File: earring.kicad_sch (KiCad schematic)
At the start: 104 parts, among them J2 USB_C_Receptacle_USB2.0, Q1 Q_NMOS_SGD, Q5 light_sensor, U1 Magnetic Switch, U10 USBLC6-2P6, U20 LGS4056H, U3 RP2040, U4 W25Q16JVUXIQ, U43 TPS22913BYZVR, U44 TPS22913BYZVR, U7 LSM6DS3, U8 DS6091AED4, U9 NCP730BMT330TBG, Y1 Crystal_GND24

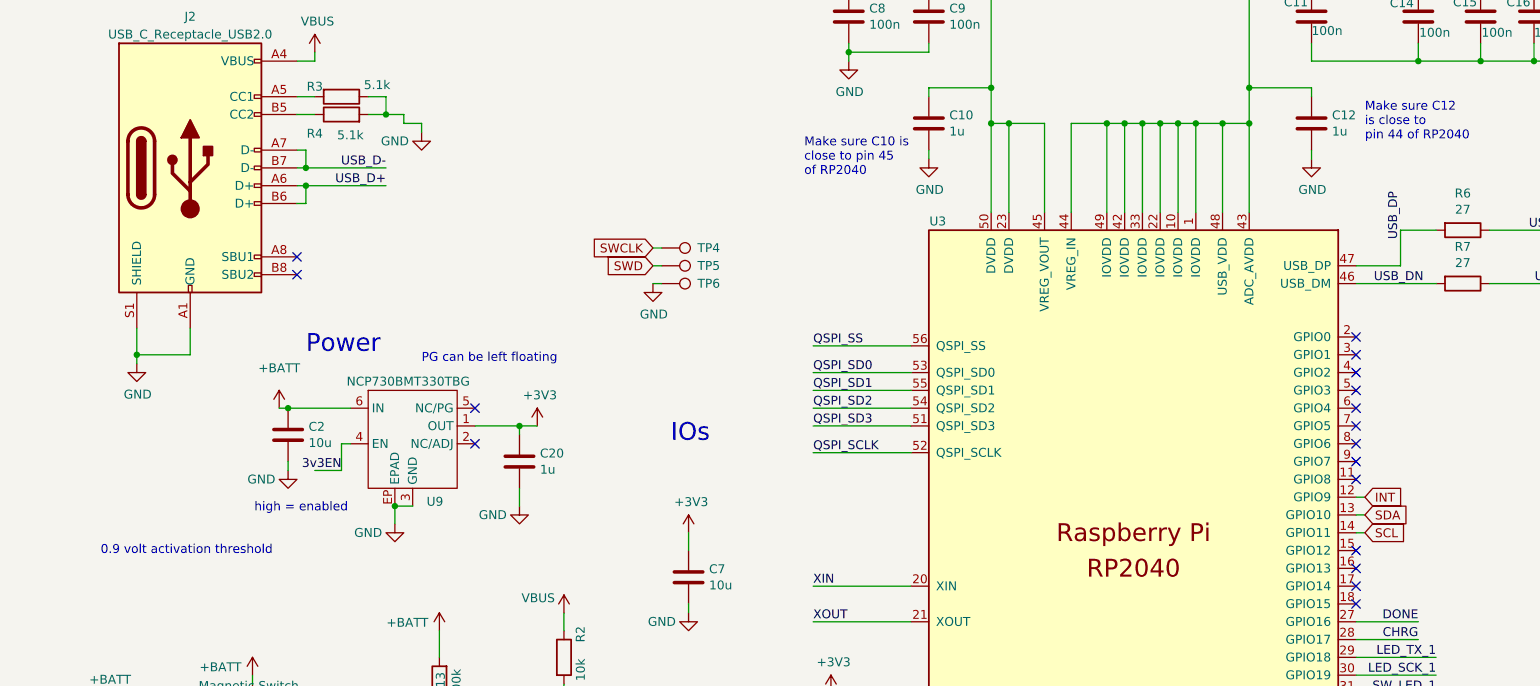
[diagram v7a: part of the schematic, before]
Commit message: updated with better clearance, ordered this rev after canceling the last order
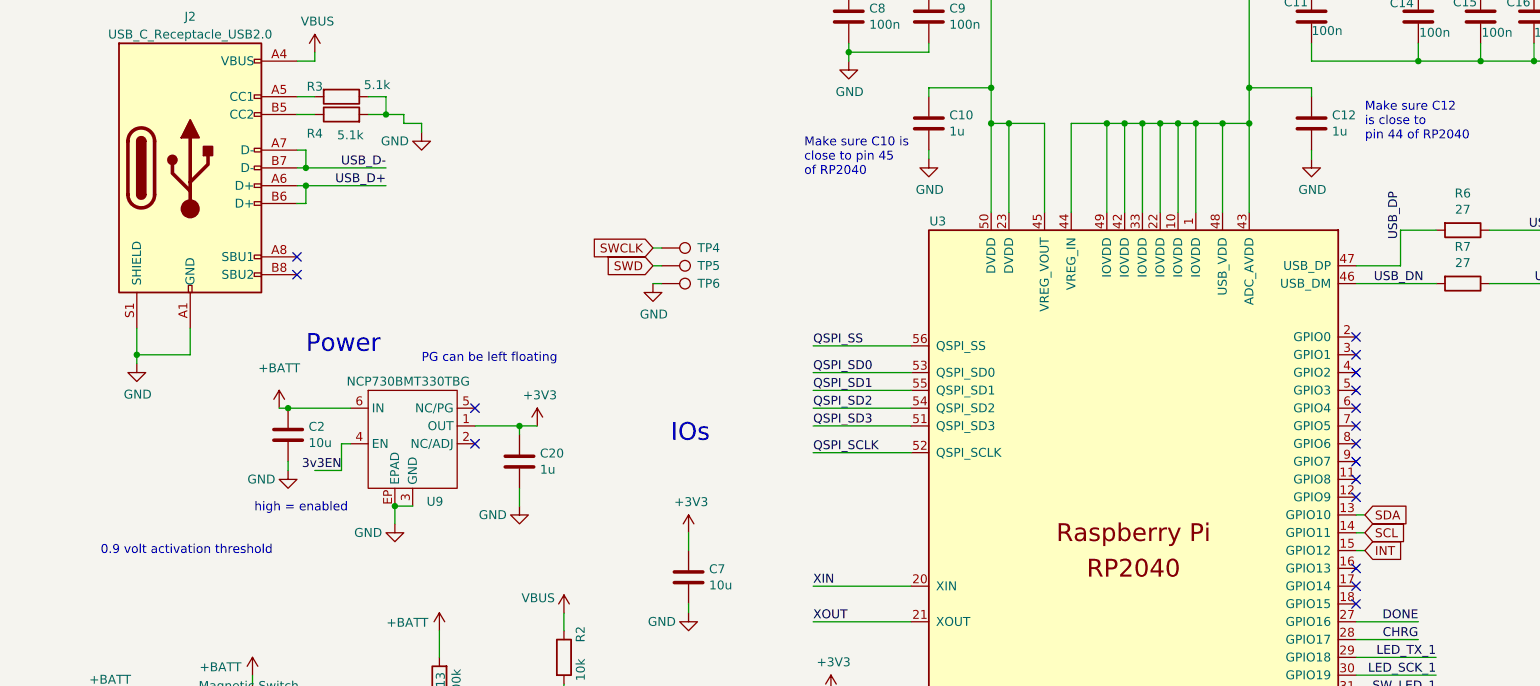
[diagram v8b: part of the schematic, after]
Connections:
- net INT: now also U3.15 (GPIO12); no longer U3.12 (GPIO9)
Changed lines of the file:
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@@
 (kicad_sch
-	(version 20231120)
+	(version 20250114)
 	(generator "eeschema")
-	(generator_version "8.0")
+	(generator_version "9.0")
 	(paper "A3")
 	(title_block
@@
 		(comment 2 "LICENSE: CERN-OHL-P")
 	)
+	(text "Make sure C10 is\nclose to pin 45\nof RP2040"
+		(exclude_from_sim no)
+		(at 127 106.68 0)
+		(effects
+			(font
+				(size 1.27 1.27)
+			)
+			(justify left bottom)
+		)
+	)
+	(text "Prevent vbus from overvoltage on BATT or 3v3EN"
+		(exclude_from_sim no)
+		(at -127 300.99 0)
+		(effects
+			(font
+				(size 1.27 1.27)
+			)
+		)
+	)
+	(text "Consider 401030 (4x10x30mm) battery cell, 120mah\nit is unclear if protection is included\nskip connector and solder battery to board"
+		(exclude_from_sim no)
+		(at 210.82 34.29 0)
+		(effects
+			(font
+				(size 1.27 1.27)
+			)
+			(justify left bottom)
+		)
+	)
+	(text "Power"
+		(exclude_from_sim no)
+		(at 54.61 80.01 0)
+		(effects
+			(font
+				(size 2.54 2.54)
+			)
+			(justify left bottom)
+		)
+	)
+	(text "Crystal"
+		(exclude_from_sim no)
+		(at 182.88 49.53 0)
+		(effects
+			(font
+				(size 2.54 2.54)
+			)
+			(justify left bottom)
+		)
+	)
+	(text "R10 sets charging current\n10k = 100 ma"
+		(exclude_from_sim no)
+		(at 31.75 62.23 0)
+		(effects
+			(font
+				(size 1.27 1.27)
+			)
+			(justify left bottom)
+		)
+	)
+	(text "IOs"
+		(exclude_from_sim no)
+		(at 107.95 144.78 0)
+		(effects
+			(font
+				(size 2.54 2.54)
+			)
+			(justify left bottom)
+		)
+	)
+	(text "Undervoltage cutoff 2.80v\nOvervoltage cutoff 4.30v"
+		(exclude_from_sim no)
+		(at 119.38 50.8 0)
+		(effects
+			(font
+				(size 1.27 1.27)
+			)
+		)
+	)
+	(text "high when no\nmagnet present\n\nlow when\nmagnet present"
+		(exclude_from_sim no)
+		(at 64.77 197.612 0)
+		(effects
+			(font
+				(size 1.27 1.27)
+			)
+		)
+	)
+	(text "Don't backfeed to vbus or usb_boot circuit fails"
+		(exclude_from_sim no)
+		(at -127 303.53 0)
+		(effects
+			(font
+				(size 1.27 1.27)
+			)
+		)
+	)
+	(text "PG can be left floating"
+		(exclude_from_sim no)
+		(at 72.39 133.35 0)
+		(effects
+			(font
+				(size 1.27 1.27)
+			)
+			(justify left bottom)
+		)
+	)
+	(text "Make sure C12\nis close to\npin 44 of RP2040"
+		(exclude_from_sim no)
+		(at 207.01 101.6 0)
+		(effects
+			(font
+				(size 1.27 1.27)
+			)
+			(justify left bottom)
+		)
+	)
+	(text "0.9 volt activation threshold"
+		(exclude_from_sim no)
+		(at 38.862 160.02 0)
+		(effects
+			(font
+				(size 1.27 1.27)
+			)
+		)
+	)
+	(text "make sure power routing with vbus, battery, and 3.3v are all correct"
+		(exclude_from_sim no)
+		(at -156.21 330.2 0)
+		(effects
+			(font
+				(size 1.27 1.27)
+			)
+			(justify left bottom)
+		)
+	)
+	(text "high = enabled"
+		(exclude_from_sim no)
+		(at 48.514 154.686 0)
+		(effects
+			(font
+				(size 1.27 1.27)
+			)
+			(justify left bottom)
+		)
+	)
+	(text "Power"
+		(exclude_from_sim no)
+		(at 55.88 132.08 0)
+		(effects
+			(font
+				(size 2.54 2.54)
+			)
+			(justify left bottom)
+		)
+	)
+	(text "buffer flips at less than 0.7v\nshould take 238ms for it to rise\nhttp://ladyada.net/library/rccalc.html"
+		(exclude_from_sim no)
+		(at -149.86 317.5 0)
+		(effects
+			(font
+				(size 1.27 1.27)
+			)
+			(justify left bottom)
+		)
+	)
+	(text "Temp floating is okay."
+		(exclude_from_sim no)
+		(at 73.66 39.37 0)
+		(effects
+			(font
+				(size 1.27 1.27)
+			)
+			(justify left bottom)
+		)
+	)
+	(text "Flash"
+		(exclude_from_sim no)
+		(at 24.13 224.79 0)
+		(effects
+			(font
+				(size 2.54 2.54)
+			)
+			(justify left bottom)
+		)
+	)
 	(junction
 		(at 133.35 88.9)
@@
 	)
 	(no_connect
-		(at 205.74 160.02)
+		(at 205.74 152.4)
 	)
 	(no_connect
@@
 	(wire
 		(pts
-			(xy 207.01 152.4) (xy 205.74 152.4)
+			(xy 207.01 160.02) (xy 205.74 160.02)
 		)
 		(stroke
@@
 		)
 	)
-	(text "Make sure C10 is\nclose to pin 45\nof RP2040"
-		(exclude_from_sim no)
-		(at 127 106.68 0)
-		(effects
-			(font
-				(size 1.27 1.27)
-			)
-			(justify left bottom)
-		)
-	)
-	(text "Prevent vbus from overvoltage on BATT or 3v3EN"
-		(exclude_from_sim no)
-		(at -127 300.99 0)
-		(effects
-			(font
-				(size 1.27 1.27)
-			)
-		)
-	)
-	(text "Consider 401030 (4x10x30mm) battery cell, 120mah\nit is unclear if protection is included\nskip connector and solder battery to board"
-		(exclude_from_sim no)
-		(at 210.82 34.29 0)
-		(effects
-			(font
-				(size 1.27 1.27)
-			)
-			(justify left bottom)
-		)
-	)
-	(text "Power"
-		(exclude_from_sim no)
-		(at 54.61 80.01 0)
-		(effects
-			(font
-				(size 2.54 2.54)
-			)
-			(justify left bottom)
-		)
-	)
-	(text "Crystal"
-		(exclude_from_sim no)
-		(at 182.88 49.53 0)
-		(effects
-			(font
-				(size 2.54 2.54)
-			)
-			(justify left bottom)
-		)
-	)
-	(text "R10 sets charging current\n10k = 100 ma"
-		(exclude_from_sim no)
-		(at 31.75 62.23 0)
-		(effects
-			(font
-				(size 1.27 1.27)
-			)
-			(justify left bottom)
-		)
-	)
-	(text "IOs"
-		(exclude_from_sim no)
-		(at 107.95 144.78 0)
-		(effects
-			(font
-				(size 2.54 2.54)
-			)
-			(justify left bottom)
-		)
-	)
-	(text "Undervoltage cutoff 2.80v\nOvervoltage cutoff 4.30v"
-		(exclude_from_sim no)
-		(at 119.38 50.8 0)
-		(effects
-			(font
-				(size 1.27 1.27)
-			)
-		)
-	)
-	(text "high when no\nmagnet present\n\nlow when\nmagnet present"
-		(exclude_from_sim no)
-		(at 64.77 197.612 0)
-		(effects
-			(font
-				(size 1.27 1.27)
-			)
-		)
-	)
-	(text "Don't backfeed to vbus or usb_boot circuit fails"
-		(exclude_from_sim no)
-		(at -127 303.53 0)
-		(effects
-			(font
-				(size 1.27 1.27)
-			)
-		)
-	)
-	(text "PG can be left floating"
-		(exclude_from_sim no)
-		(at 72.39 133.35 0)
-		(effects
-			(font
-				(size 1.27 1.27)
-			)
-			(justify left bottom)
-		)
-	)
-	(text "Make sure C12\nis close to\npin 44 of RP2040"
-		(exclude_from_sim no)
-		(at 207.01 101.6 0)
-		(effects
-			(font
-				(size 1.27 1.27)
-			)
-			(justify left bottom)
-		)
-	)
-	(text "0.9 volt activation threshold"
-		(exclude_from_sim no)
-		(at 38.862 160.02 0)
-		(effects
-			(font
-				(size 1.27 1.27)
-			)
-		)
-	)
-	(text "make sure power routing with vbus, battery, and 3.3v are all correct"
-		(exclude_from_sim no)
-		(at -156.21 330.2 0)
-		(effects
-			(font
-				(size 1.27 1.27)
-			)
-			(justify left bottom)
-		)
-	)
-	(text "high = enabled"
-		(exclude_from_sim no)
-		(at 48.514 154.686 0)
-		(effects
-			(font
-				(size 1.27 1.27)
-			)
-			(justify left bottom)
-		)
-	)
-	(text "Power"
-		(exclude_from_sim no)
-		(at 55.88 132.08 0)
-		(effects
-			(font
-				(size 2.54 2.54)
-			)
-			(justify left bottom)
-		)
-	)
-	(text "buffer flips at less than 0.7v\nshould take 238ms for it to rise\nhttp://ladyada.net/library/rccalc.html"
-		(exclude_from_sim no)
-		(at -149.86 317.5 0)
-		(effects
-			(font
-				(size 1.27 1.27)
-			)
-			(justify left bottom)
-		)
-	)
-	(text "Temp floating is okay."
-		(exclude_from_sim no)
-		(at 73.66 39.37 0)
-		(effects
-			(font
-				(size 1.27 1.27)
-			)
-			(justify left bottom)
-		)
-	)
-	(text "Flash"
-		(exclude_from_sim no)
-		(at 24.13 224.79 0)
-		(effects
-			(font
-				(size 2.54 2.54)
-			)
-			(justify left bottom)
-		)
-	)
 	(label "LED_1_V"
 		(at 382.27 176.53 0)
@@
 	(global_label "INT"
 		(shape input)
-		(at 207.01 152.4 0)
+		(at 207.01 160.02 0)
 		(fields_autoplaced yes)
 		(effects
@@
 		)
 		(property "Intersheetrefs" "${INTERSHEET_REFS}"
-			(at 212.2439 152.4 0)
+			(at 212.2439 160.02 0)
 			(effects
 				(font
@@
 		)
 	)
+	(embedded_fonts no)
 )
